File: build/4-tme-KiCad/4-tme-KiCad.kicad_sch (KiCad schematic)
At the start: 29 parts, among them J1 MIDI IN, SW1 RotaryEncoder, SW10 RotaryEncoder, SW11 RotaryEncoder, SW12 RotaryEncoder, SW13 RotaryEncoder, SW14 RotaryEncoder, SW15 RotaryEncoder, SW16 RotaryEncoder, SW2 RotaryEncoder, SW3 RotaryEncoder, SW4 RotaryEncoder, SW5 RotaryEncoder, SW6 RotaryEncoder, SW7 RotaryEncoder, SW8 RotaryEncoder, SW9 RotaryEncoder, U1 CD74HC4067M, U2 CD74HC4067M, U3 6N137

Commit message: REV1
Encoders + MUX
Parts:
- added C10, C11, C12, C13, C14, C15, C16, C17, C18, C19, C20, C21, C22, C23, C24, C25, C26, C27, C28, C29, C30, C31, C32, C33, C34, C4, C5, C6, C7, C8, C9: 10nF_0603_25V, Capacitor_SMD:C_0201_0603Metric, symbol PCM_4ms_Capacitor:10nF_0603_25V
- added R10, R11, R12, R13, R14, R15, R16, R17, R18, R19, R20, R21, R22, R23, R24, R25, R26, R27, R28, R29, R30, R31, R32, R33, R34, R35, R36, R37, R38, R39, R40, R41, R42, R43, R44, R45, R46, R47, R48, R49, R5, R50, R51, R52, R53, R54, R55, R56, R57, R58, R59, R6, R60, R61, R62, R63, R64, R65, R66, R67, R7, R8, R9: 10k_0603_0.1%, 4ms_Resistor:R_0603, symbol PCM_4ms_Resistor:10k_0603_0.1%
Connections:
- net D3V3: now also R11.1, R12.1, R15.1, R16.1, R19.1, R20.1, R23.1, R24.1, R27.1, R28.1, R31.1, R32.1, R35.1, R36.1, R39.1, R40.1, R43.1, R44.1, R47.1, R48.1, R5.1, R51.1, R52.1, R55.1, R56.1, R59.1, R6.1, R60.1, R63.1, R64.1, R67.1, R8.1
- net DGND: now also C10.2, C11.2, C12.2, C13.2, C14.2, C15.2, C16.2, C17.2, C18.2, C19.2, C20.2, C21.2, C22.2, C23.2, C24.2, C25.2, C26.2, C27.2, C28.2, C29.2, C30.2, C31.2, C32.2, C33.2, C34.2, C4.2, C5.2, C6.2, C7.2, C8.2, C9.2
- net C16: now reaches SW9.A
- net C16: now also U2.9 (I0), R36.2, R37.1
- net C17: now reaches SW9.B
- net C17: now also U2.8 (I1), R38.1, R39.2
- net C18: now reaches SW10.A
- net C18: now also U2.7 (I2), R40.2, R41.1
- net C19: now reaches SW10.B
- net C19: now also U2.6 (I3), R42.1, R43.2
- net C8: now reaches SW5.A
- net C8: now also U1.23 (I8), R20.2, R21.1
- net C9: now reaches SW5.B
- net C9: now also U1.22 (I9), R22.1, R23.2
- net C14: now reaches SW8.A
- net C14: now also U1.17 (I14), R32.2, R33.1
- net C15: now reaches SW8.B
- net C15: now also U1.16 (I15), R34.1, R35.2
- net C26: now reaches SW14.A
- net C26: now also U2.21 (I10), R56.2, R57.1
- net C27: now reaches SW14.B
- net C27: now also U2.20 (I11), R58.1, R59.2
- net C22: now reaches SW12.A
- net C22: now also U2.3 (I6), R48.2, R49.1
- net C23: now reaches SW12.B
- net C23: now also U2.2 (I7), R50.1, R51.2
- net C20: now reaches SW11.A
- net C20: now also U2.5 (I4), R44.2, R45.1
- net C21: now reaches SW11.B
- net C21: now also U2.4 (I5), R46.1, R47.2
- net C31: now reaches U2.16 (I15)
- net C31: now also SW16.B, R66.1, R67.2
- net C30: now reaches U2.17 (I14)
- net C30: now also SW16.A, R64.2, R65.1
- net C29: now reaches U2.18 (I13)
- net C29: now also SW15.B, R62.1, R63.2
- net C28: now reaches U2.19 (I12)
- net C28: now also SW15.A, R60.2, R61.1
- net C25: now reaches U2.22 (I9)
- net C25: now also SW13.B, R54.1, R55.2
- net C24: now reaches U2.23 (I8)
- net C24: now also SW13.A, R52.2, R53.1
- net C4: now reaches SW3.A
- net C4: now also U1.5 (I4), R12.2, R13.1
- net C5: now reaches SW3.B
- net C5: now also U1.4 (I5), R14.1, R15.2
- net C10: now reaches SW6.A
- net C10: now also U1.21 (I10), R24.2, R25.1
- net C11: now reaches SW6.B
- net C11: now also U1.20 (I11), R26.1, R27.2
- net C6: now reaches SW4.A
- net C6: now also U1.3 (I6), R16.2, R17.1
- net C7: now reaches SW4.B
- net C7: now also U1.2 (I7), R18.1, R19.2
- net C13: now reaches U1.18 (I13)
- net C13: now also SW7.B, R30.1, R31.2
- net C12: now reaches U1.19 (I12)
- net C12: now also SW7.A, R28.2, R29.1
- net C3: now reaches U1.6 (I3)
- net C3: now also SW2.B, R10.1, R11.2
- net C2: now reaches U1.7 (I2)
- net C2: now also SW2.A, R8.2, R9.1
- net C1: now reaches U1.8 (I1)
- net C1: now also SW1.B, R6.2, R7.1
- net C0: now reaches U1.9 (I0)
- net C0: now also R4.1, SW1.A, R5.2
- net at SW1.C: no longer R4.1
- new net: C8.1, R14.2
- new net: C29.1, R57.2
- new net: C27.1, R53.2
- new net: C24.1, R46.2
- new net: C21.1, R41.2
- new net: C9.1, R17.2
- new net: C26.1, R50.2
- new net: C4.1, R7.2
- new net: C30.1, R58.2
- new net: C6.1, R10.2
- new net: C15.1, R29.2
- new net: C14.1, R26.2
- new net: C20.1, R38.2
- new net: C16.1, R30.2
- new net: C5.1, R9.2
- new net: C11.1, R21.2
- new net: C7.1, R13.2
- new net: C28.1, R54.2
- new net: C25.1, R49.2
- new net: C22.1, R42.2
- new net: C23.1, R45.2
- new net: C18.1, R34.2
- new net: C13.1, R25.2
- new net: C34.1, R66.2
- new net: C12.1, R22.2
- new net: C10.1, R18.2
- new net: C33.1, R65.2
- new net: C31.1, R61.2
- new net: C32.1, R62.2
- new net: C17.1, R33.2
- new net: C19.1, R37.2
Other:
- moved on the sheet: C3, R4, SW1

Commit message: Update 4-tme-KiCad.kicad_sch
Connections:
- net MUX1_SIG: now also A1.22 (ADC_0)
- net MUX2_SIG: now also A1.23 (ADC_1); no longer U2.1 (COM)
- net S0: now also A1.1 (USB_ID)
- net S1: now also A1.2 (SD_DATA_3)
- net S2: now also A1.3 (SD_DATA_2)
- net S3: now also A1.4 (SD_DATA_1)

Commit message: rev1
encoders revision 3
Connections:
- net C0: now also C3.1, R4.2; no longer R4.1, R5.2, SW1.A
- net C1: now also C4.1, R7.2; no longer R6.2, R7.1, SW1.B
- net C10: now also C13.1, R25.2; no longer R24.2, R25.1, SW6.A
- net C11: now also C14.1, R26.2; no longer R26.1, R27.2, SW6.B
- net C12: now also C15.1, R29.2; no longer R28.2, R29.1, SW7.A
- net C13: now also C16.1, R30.2; no longer R30.1, R31.2, SW7.B
- net C14: now also C17.1, R33.2; no longer R32.2, R33.1, SW8.A
- net C15: now also C18.1, R34.2; no longer R34.1, R35.2, SW8.B
- net C16: now also C19.1, R37.2; no longer R36.2, R37.1, SW9.A
- net C17: now also C20.1, R38.2; no longer R38.1, R39.2, SW9.B
- net C18: now also C21.1, R41.2; no longer R40.2, R41.1, SW10.A
- net C19: now also C22.1, R42.2; no longer R42.1, R43.2, SW10.B
- net C2: now also C5.1, R9.2; no longer R8.2, R9.1, SW2.A
- net C20: now also C23.1, R45.2; no longer R44.2, R45.1, SW11.A
- net C21: now also C24.1, R46.2; no longer R46.1, R47.2, SW11.B
- net C22: now also C25.1, R49.2; no longer R48.2, R49.1, SW12.A
- net C23: now also C26.1, R50.2; no longer R50.1, R51.2, SW12.B
- net C24: now also C27.1, R53.2; no longer R52.2, R53.1, SW13.A
- net C25: now also C28.1, R54.2; no longer R54.1, R55.2, SW13.B
- net C26: now also C29.1, R57.2; no longer R56.2, R57.1, SW14.A
- net C27: now also C30.1, R58.2; no longer R58.1, R59.2, SW14.B
- net C28: now also C31.1, R61.2; no longer R60.2, R61.1, SW15.A
- net C29: now also C32.1, R62.2; no longer R62.1, R63.2, SW15.B
- net C3: now also C6.1, R10.2; no longer R10.1, R11.2, SW2.B
- net C30: now also C33.1, R65.2; no longer R64.2, R65.1, SW16.A
- net C31: now also C34.1, R66.2; no longer R66.1, R67.2, SW16.B
- net C4: now also C7.1, R13.2; no longer R12.2, R13.1, SW3.A
- net C5: now also C8.1, R14.2; no longer R14.1, R15.2, SW3.B
- net C6: now also C9.1, R17.2; no longer R16.2, R17.1, SW4.A
- net C7: now also C10.1, R18.2; no longer R18.1, R19.2, SW4.B
- net C8: now also C11.1, R21.2; no longer R20.2, R21.1, SW5.A
- net C9: now also C12.1, R22.2; no longer R22.1, R23.2, SW5.B
- net DGND: now also SW1.C, SW10.C, SW11.C, SW12.C, SW13.C, SW14.C, SW15.C, SW16.C, SW2.C, SW3.C, SW4.C, SW5.C, SW6.C, SW7.C, SW8.C, SW9.C
- new net: R16.2, R17.1, SW4.A
- new net: R62.1, R63.2, SW15.B
- new net: R34.1, R35.2, SW8.B
- new net: R46.1, R47.2, SW11.B
- new net: R40.2, R41.1, SW10.A
- new net: R50.1, R51.2, SW12.B
- new net: R52.2, R53.1, SW13.A
- new net: R54.1, R55.2, SW13.B
- new net: R58.1, R59.2, SW14.B
- new net: R36.2, R37.1, SW9.A
- new net: R38.1, R39.2, SW9.B
- new net: R10.1, R11.2, SW2.B
- new net: R56.2, R57.1, SW14.A
- new net: R28.2, R29.1, SW7.A
- new net: R60.2, R61.1, SW15.A
- new net: R30.1, R31.2, SW7.B
- new net: R32.2, R33.1, SW8.A
- new net: R48.2, R49.1, SW12.A
- new net: R8.2, R9.1, SW2.A
- new net: R6.2, R7.1, SW1.B
- new net: R12.2, R13.1, SW3.A
- new net: R64.2, R65.1, SW16.A
- new net: R66.1, R67.2, SW16.B
- new net: R4.1, R5.2, SW1.A
- new net: R18.1, R19.2, SW4.B
- new net: R26.1, R27.2, SW6.B
- new net: R44.2, R45.1, SW11.A
- new net: R20.2, R21.1, SW5.A
- new net: R22.1, R23.2, SW5.B
- new net: R24.2, R25.1, SW6.A
- new net: R14.1, R15.2, SW3.B
- new net: R42.1, R43.2, SW10.B

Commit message: Update 4-tme-KiCad.kicad_sch
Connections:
- net A3V3: no longer C1.1, C2.1, U1.24 (VCC), U2.24 (VCC)
- net AGND: no longer C1.2, C2.2, U1.12 (GND), U1.15 (~{E}), U2.12 (GND), U2.15 (~{E})
- net D3V3: now also C1.1, C2.1, U1.24 (VCC), U2.24 (VCC)
- net DGND: now also C1.2, C2.2, U1.12 (GND), U1.15 (~{E}), U2.12 (GND), U2.15 (~{E})
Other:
- note added: "ENCODERS"
- note added: "MUX"

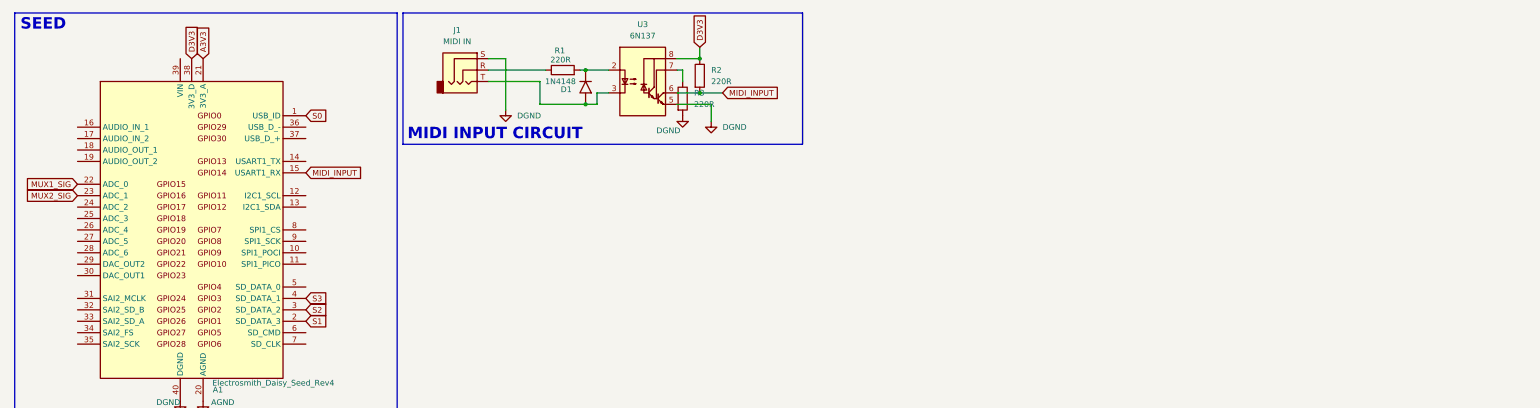
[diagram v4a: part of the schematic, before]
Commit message: PCB update
-fixed oled orientation
- fixed resistor descriptor inconsistencies
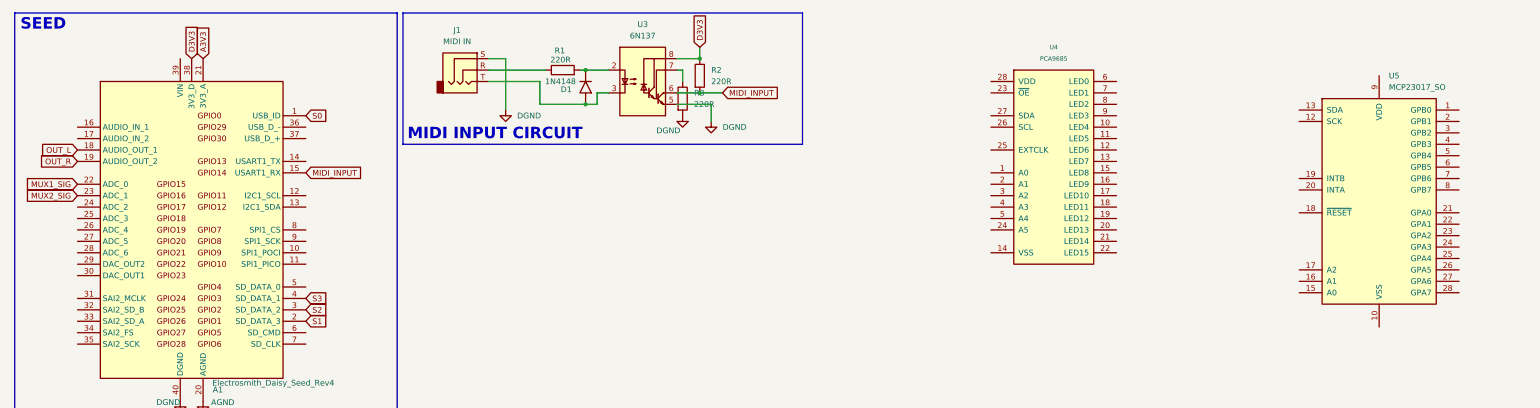
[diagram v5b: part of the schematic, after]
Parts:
- added U4: PCA9685, 4ms_Package_SSOP:TSSOP-28_4.4x9.7mm_Pitch0.65mm, symbol PCM_4ms_IC:PCA9685
- added U5: MCP23017_SO, Package_SO:SOIC-28W_7.5x17.9mm_P1.27mm, symbol Interface_Expansion:MCP23017_SO
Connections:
- net OUT_L: now reaches A1.18 (AUDIO_OUT_1)
- net OUT_R: now reaches A1.19 (AUDIO_OUT_2)

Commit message: pcb
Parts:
- added C35, C36, C37, C38, C39, C40, C41: 10nF_0603_25V, Capacitor_SMD:C_0201_0603Metric, symbol PCM_4ms_Capacitor:10nF_0603_25V
- added D10, D11, D12, D13, D14, D15, D2, D3, D4, D5, D6, D7, D8, D9: LED_5mm, LED_THT:LED_D5.0mm, symbol PCM_SL_Devices:LED_5mm
- added R68, R69, R70, R71: 10k_0603_0.1%, 4ms_Resistor:R_0603, symbol PCM_4ms_Resistor:10k_0603_0.1%
- added R72, R73, R74, R75, R76, R77, R78, R79, R80, R81, R82, R83, R84, R85: 470R_0603, PCM_Resistor_SMD_AKL:R_0603_1608Metric_Pad0.98x0.95mm, symbol PCM_4ms_Resistor:470R_0603
- added R86, R87: 4.7k_0603, PCM_Resistor_SMD_AKL:R_0201_0603Metric_Pad0.64x0.40mm, symbol PCM_4ms_Resistor:4.7k_0603
- added RV1, RV2, RV3: R_Potentiometer, PCM_Potentiometer_THT_AKL:Potentiometer_Alps_RK09K_Single_Vertical, symbol Device:R_Potentiometer
- added SW17: RotaryEncoder, rotaryencoder:RotaryEncoder, symbol Device:RotaryEncoder
- added U6: CD74HC4067M, Package_SO:SOIC-24W_7.5x15.4mm_P1.27mm, symbol 74xx:CD74HC4067M
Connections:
- net C30: now also C36.1, R69.2
- net C31: now also C37.1, R70.2
- net D3V3: now also U4.28 (VDD), C35.1, C41.1, R68.1, R71.1, R72.2, R73.2, R74.2, R75.2, R76.2, R77.2, R78.2, R79.2, R80.2, R81.2, R82.2, R83.2, R84.2, R85.2, R86.1, R87.1, RV1.3, RV2.3, RV3.3, U6.24 (VCC)
- net DGND: now also U4.1 (A0), U4.14 (VSS), U4.2 (A1), U4.23 (~{OE}), U4.24 (A5), U4.25 (EXTCLK), U4.3 (A2), U4.4 (A3), U4.5 (A4), C35.2, C36.2, C37.2, C38.2, C39.2, C40.2, C41.2, RV1.1, RV2.1, RV3.1, SW17.C, U6.12 (GND), U6.15 (~{E})
- net MUX2_SIG: now also U2.1 (COM)
- net S0: now also U6.10 (S0)
- net S1: now also U6.11 (S1)
- net S2: now also U6.14 (S2)
- net S3: now also U6.13 (S3)
- net at U4.10 (LED4): now also D6.1
- net at U4.11 (LED5): now also D7.1
- net at U4.12 (LED6): now also D8.1
- net at U4.13 (LED7): now also D9.1
- net at U4.15 (LED8): now also D10.1
- net at U4.16 (LED9): now also D11.1
- net at U4.17 (LED10): now also D12.1
- net at U4.18 (LED11): now also D13.1
- net at U4.19 (LED12): now also D14.1
- net at U4.20 (LED13): now also D15.1
- net SCL: now reaches U4.26 (SCL)
- net SCL: now also R87.2
- net SDA: now reaches U4.27 (SDA)
- net SDA: now also R86.2
- net at U4.6 (LED0): now also D2.1
- net at U4.7 (LED1): now also D3.1
- net at U4.8 (LED2): now also D4.1
- net at U4.9 (LED3): now also D5.1
- new net: D10.2, R80.1
- new net: D6.2, R76.1
- new net: D12.2, R82.1
- new net: D2.2, R72.1
- new net: R68.2, R69.1, SW17.A
- new net: R70.1, R71.2, SW17.B
- new net: D5.2, R75.1
- new net: D13.2, R83.1
- new net: D14.2, R84.1
- new net: D7.2, R77.1
- new net: D4.2, R74.1
- new net: D8.2, R78.1
- new net: D3.2, R73.1
- new net: D15.2, R85.1
- new net: D9.2, R79.1
- new net: D11.2, R81.1
- new net DELAY_LEVEL: C39.1, RV2.2, U6.6 (I3)
- new net DELAY_SPEED: C38.1, RV1.2, U6.7 (I2)
- new net DISTORTION: C40.1, RV3.2, U6.5 (I4)
- new net MENU_ENC_A: U6.9 (I0)
- new net MENU_ENC_B: U6.8 (I1)
- no-connect marks 0 -> 2
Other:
- note added: "-1"
- note added: "-2"
- note added: "0"
- note added: "1"
- note added: "2"
- note added: "ATTACK"
- note added: "CUTOFF"
- note added: "DECAY"
- note added: "DELAY LEVEL"
- note added: "DELAY SPEED"
- note added: "DISTORTION"
- note added: "FILT LFO"
- note added: "FILT. CV"
- note added: "FILT. ENV"
- note added: "LEVEL"
- note added: "LFO RATE"
- note added: "MAIN ENC"
- note added: "PAN"
- note added: "PITCH ENV"
- note added: "PITCH LFO"
- note added: "POTENTIOMETERS"
- note added: "RELEASE"
- note added: "RESONANCE"
- note added: "SUSTAIN"
- note added: "TUNE"
- note added: "VOICE 1"
- note added: "VOICE 2"
- note added: "VOICE 3"
- note added: "VOICE 4"
- note added: "WAVEFORM"
- note added: "delay"
- note added: "pulse"
- note added: "saw"
- note added: "sqr"
- note added: "tri"
- moved on the sheet: U4

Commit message: PITCH CV
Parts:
- added C42, C43, C44, C45: 10nF_0603_25V, Capacitor_SMD:C_0201_0603Metric, symbol PCM_4ms_Capacitor:10nF_0603_25V
- added J2: PITCH CV 1, symbol Connector_Audio:AudioJack3
- added J3: PITCH CV 2, symbol Connector_Audio:AudioJack3
- added J4, J5: PITCH CV 3, symbol Connector_Audio:AudioJack3
- added R88, R89, R90, R91: 100k, Resistor_SMD:R_0201_0603Metric, symbol Device:R
- added R92, R93, R94, R95: 33k, Resistor_SMD:R_0201_0603Metric, symbol Device:R
- added R96, R97, R98, R99: 1k, Resistor_SMD:R_0201_0603Metric, symbol Device:R
- added U7: MCP6004, Package_SO:SOIC-14_3.9x8.7mm_P1.27mm, symbol Amplifier_Operational:MCP6004
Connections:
- net A3V3: now also U7.4 (V+)
- net AGND: now also C42.2, C43.2, C44.2, C45.2, J2.R, J2.S, J3.R, J3.S, J4.R, J4.S, J5.R, J5.S, R92.2, R93.2, R94.2, R95.2, U7.11 (V-)
- new net: J2.T, R88.1
- new net: R88.2, R92.1, U7.3 (+)
- new net: R90.2, R94.1, U7.10 (+)
- new net: R98.1, U7.8, U7.9 (-)
- new net: R91.2, R95.1, U7.12 (+)
- new net: R89.2, R93.1, U7.5 (+)
- new net: R96.1, U7.1, U7.2 (-)
- new net: R97.1, U7.6 (-), U7.7
- new net: R99.1, U7.13 (-), U7.14
- new net: J5.T, R91.1
- new net: J4.T, R90.1
- new net: J3.T, R89.1
- new net PITCH_CV_1: C42.1, R96.2
- new net PITCH_CV_2: C43.1, R97.2
- new net PITCH_CV_3: C44.1, C45.1, R98.2, R99.2
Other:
- note added: "CV & GATE INPUT"
- moved on the sheet: C10, C11, C12, C13, C14, C15, C16, C17, C18, C19, C20, C21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

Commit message: Pitch CV inputs
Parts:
- J5: value PITCH CV 3 -> PITCH CV 4
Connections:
- net PITCH_CV_1: now also U6.4 (I5)
- net PITCH_CV_2: now also U6.3 (I6)
- net PITCH_CV_3: now also U6.2 (I7); no longer C45.1, R99.2
- net PITCH_CV_4: now reaches U6.23 (I8)
- net PITCH_CV_4: now also C45.1, R99.2
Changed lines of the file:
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@@
 		)
 	)
-	(global_label "PITCH_CV_3"
+	(global_label "PITCH_CV_4"
 		(shape input)
 		(at 181.61 245.11 0)
@@
 		)
 	)
+	(global_label "PITCH_CV_1"
+		(shape input)
+		(at 52.07 217.17 0)
+		(fields_autoplaced yes)
+		(effects
+			(font
+				(size 1.27 1.27)
+			)
+			(justify left)
+		)
+		(property "Intersheetrefs" "${INTERSHEET_REFS}"
+			(at 66.0014 217.17 0)
+			(effects
+				(font
+					(size 1.27 1.27)
+				)
+				(justify left)
+				(hide yes)
+			)
+		)
+	)
 	(global_label "D3V3"
 		(shape input)
@@
 		)
 	)
+	(global_label "PITCH_CV_4"
+		(shape input)
+		(at 52.07 224.79 0)
+		(fields_autoplaced yes)
+		(effects
+			(font
+				(size 1.27 1.27)
+			)
+			(justify left)
+		)
+		(property "Intersheetrefs" "${INTERSHEET_REFS}"
+			(at 66.0014 224.79 0)
+			(effects
+				(font
+					(size 1.27 1.27)
+				)
+				(justify left)
+				(hide yes)
+			)
+		)
+	)
 	(global_label "D3V3"
 		(shape input)
@@
 		)
 	)
+	(global_label "PITCH_CV_3"
+		(shape input)
+		(at 52.07 222.25 0)
+		(fields_autoplaced yes)
+		(effects
+			(font
+				(size 1.27 1.27)
+			)
+			(justify left)
+		)
+		(property "Intersheetrefs" "${INTERSHEET_REFS}"
+			(at 66.0014 222.25 0)
+			(effects
+				(font
+					(size 1.27 1.27)
+				)
+				(justify left)
+				(hide yes)
+			)
+		)
+	)
 	(global_label "C2"
 		(shape input)
@@
 		)
 	)
+	(global_label "PITCH_CV_2"
+		(shape input)
+		(at 52.07 219.71 0)
+		(fields_autoplaced yes)
+		(effects
+			(font
+				(size 1.27 1.27)
+			)
+			(justify left)
+		)
+		(property "Intersheetrefs" "${INTERSHEET_REFS}"
+			(at 66.0014 219.71 0)
+			(effects
+				(font
+					(size 1.27 1.27)
+				)
+				(justify left)
+				(hide yes)
+			)
+		)
+	)
 	(global_label "D3V3"
 		(shape input)
@@
 			)
 		)
-		(property "Value" "PITCH CV 3"
+		(property "Value" "PITCH CV 4"
 			(at 130.175 233.68 0)
 			(effects
